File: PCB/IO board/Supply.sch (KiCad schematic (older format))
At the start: 29 parts

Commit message: Schematics Rev 1.0
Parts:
- gave numbers to parts that had none: 29
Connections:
- net +5V_Buck: no longer names the net of C612.1, C613.1, L604.2, U602.7 (VIN)
- net +5V_Buck: no longer U602.2 (EN)
- new net +3V3_EN: U602.2 (EN)

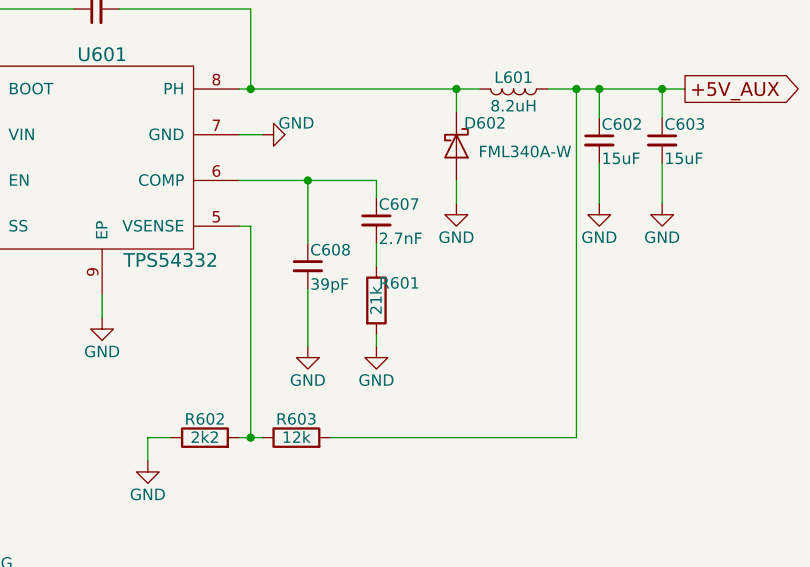
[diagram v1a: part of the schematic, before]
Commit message: Component Placement - No pul-up
ALmost finished component placement expect for pull ups and low pass
filters for switches etc
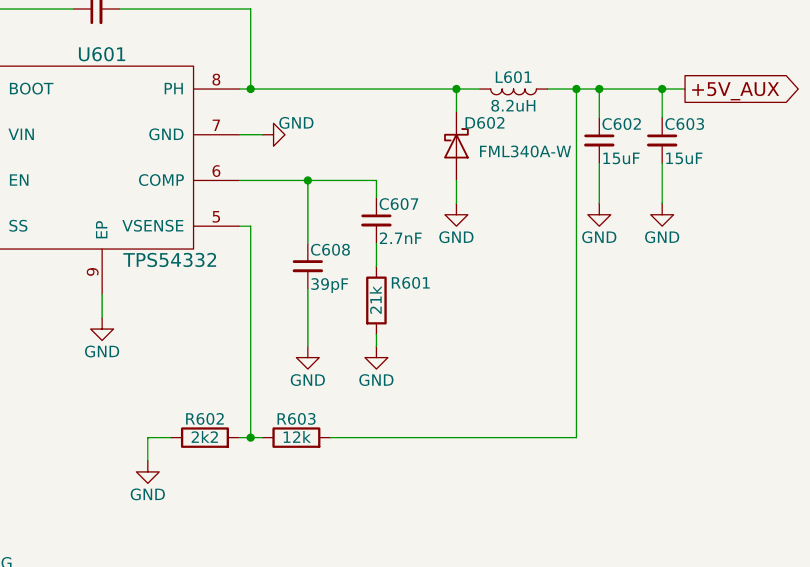
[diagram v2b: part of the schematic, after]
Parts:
- C601, C602, C603, C604, C607, C608, C609, C611, C613, C614: footprint (none) -> Capacitors_SMD:C_0603
- C605, C606: footprint (none) -> Capacitors_SMD:C_1210
- C610, C612: footprint (none) -> Capacitors_SMD:C_0805
- D601: footprint (none) -> Diode:SMD-4
- D602: footprint (none) -> Diodes_SMD:D_SMA
- D603: footprint (none) -> Diodes_SMD:D_SMB
- F601, R601, R602, R603: footprint (none) -> Resistors_SMD:R_0603
- J601: footprint (none) -> Connectors:BARREL_JACK
- J602: footprint (none) -> ELECTROMECH:Mill-Max_0990
- L601: footprint (none) -> Inductors_SMD:L_Taiyo-Yuden_NR-60xx_HandSoldering
- L602, L604: footprint (none) -> Inductors_SMD:L_0603
- L603: footprint (none) -> Inductors_SMD:L_0805
- U601: footprint (none) -> Housings_SOIC:TI_SO-PowerPAD-8_ThermalVias
- U602: footprint (none) -> Housings_DFN_QFN:DFN-8-1EP_2x2mm_Pitch0.5mm
